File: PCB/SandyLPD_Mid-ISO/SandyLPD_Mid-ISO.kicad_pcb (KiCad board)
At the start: 2 copper layers, 42.5 x 23.2 mm, 30 parts

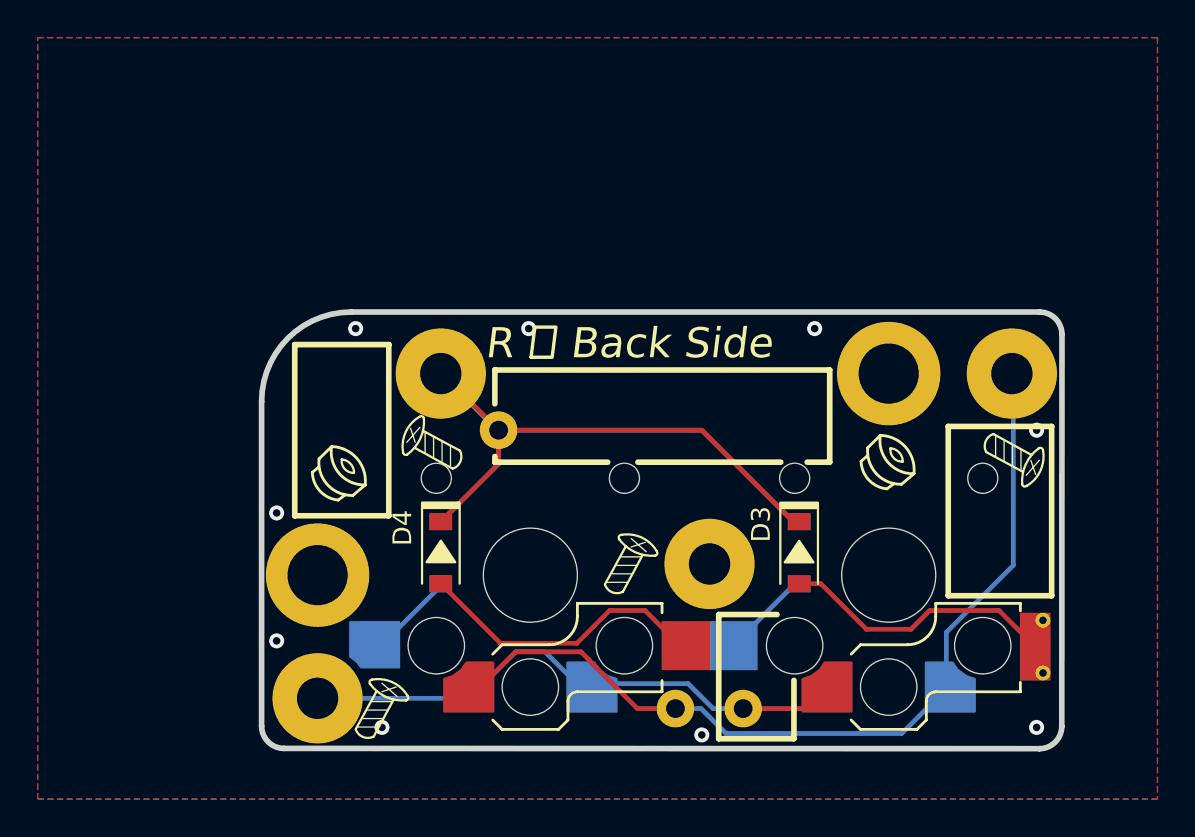
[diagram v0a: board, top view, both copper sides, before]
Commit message: ゴムシート貼り付け指標を調整
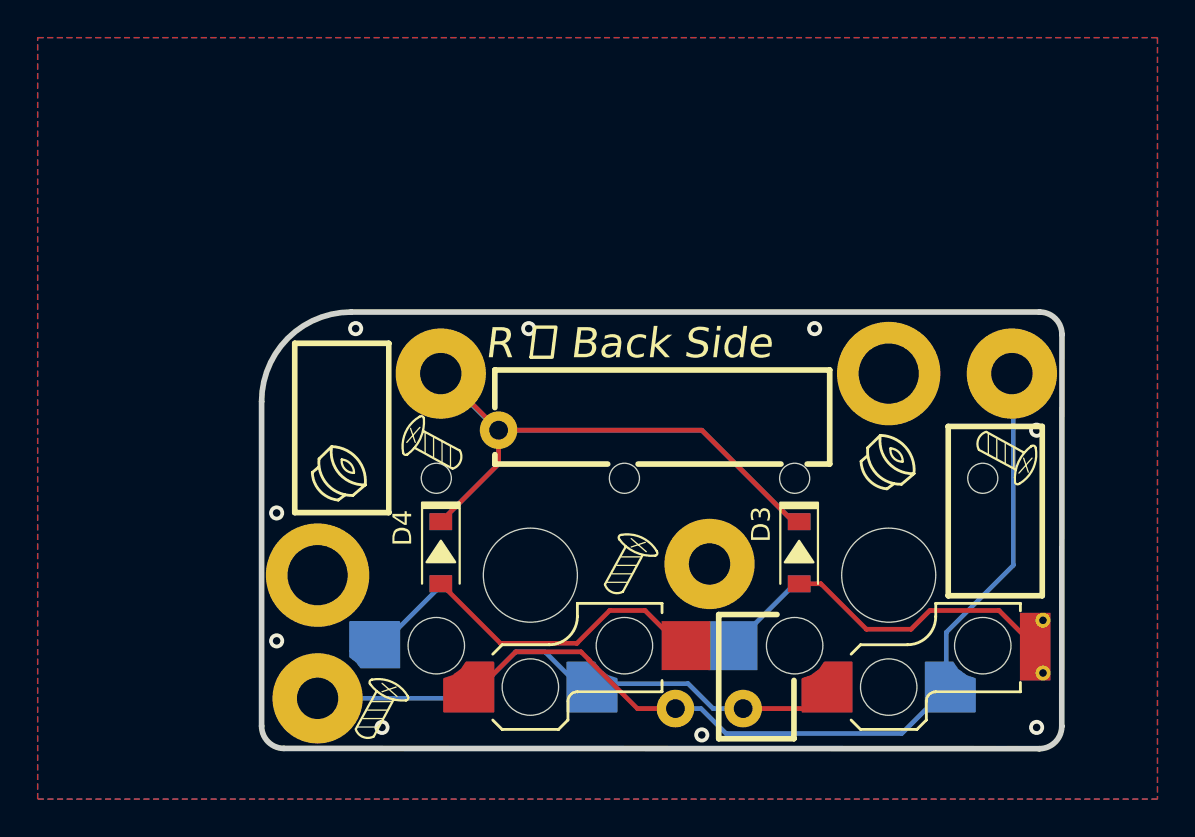
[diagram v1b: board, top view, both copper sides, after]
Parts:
- moved REF** 0.41 mm to (62.9, 43.3)
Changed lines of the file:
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@@
 		(locked yes)
 		(layer "F.Cu")
-		(at 63.241452 43.431721 -90)
+		(at 62.853952 43.312971 -90)
 		(property "Reference" "REF**"
 			(at 0 0.5 90)
@@
 	)
 	(gr_line
-		(start 38.220935 40.51903)
+		(start 38.220935 40.71903)
 		(end 38.220935 38.71903)
 		(stroke
@@
 	)
 	(gr_line
-		(start 38.220935 43.61903)
-		(end 44.220935 43.61903)
+		(start 38.220935 43.71903)
+		(end 44.220935 43.71903)
 		(stroke
 			(width 0.3)
@@
 	)
 	(gr_rect
-		(start 27.583435 37.35028)
-		(end 32.583435 46.45028)
+		(start 27.583435 37.30028)
+		(end 32.583435 46.30028)
 		(stroke
 			(width 0.3)
@@
 	(gr_line
 		(start 65.220935 44.41903)
-		(end 67.820935 44.41903)
+		(end 67.320935 44.41903)
 		(stroke
 			(width 0.3)
@@
 	)
 	(gr_line
-		(start 67.820935 44.41903)
-		(end 67.820935 51.51903)
+		(start 67.320935 44.41903)
+		(end 67.320935 51.40028)
 		(stroke
 			(width 0.3)
@@
 	)
 	(gr_line
-		(start 38.220935 43.31903)
-		(end 38.220935 43.61903)
+		(start 38.220935 43.21903)
+		(end 38.220935 43.71903)
 		(stroke
 			(width 0.3)
@@
 	)
 	(gr_line
-		(start 67.873435 51.36028)
-		(end 67.873435 52.66028)
-		(stroke
-			(width 0.2)
-			(type default)
-		)
-		(layer "B.SilkS")
-	)
-	(gr_line
 		(start 62.320935 53.81903)
 		(end 62.320935 44.41903)
@@
 	)
 	(gr_line
-		(start 45.820935 43.61903)
-		(end 53.420935 43.61903)
+		(start 45.833435 43.71903)
+		(end 53.433435 43.71903)
 		(stroke
 			(width 0.3)
@@
 	)
 	(gr_line
-		(start 54.820935 43.61903)
-		(end 56.020935 43.61903)
+		(start 54.820935 43.71903)
+		(end 56.020935 43.71903)
 		(stroke
 			(width 0.3)
@@
 	)
 	(gr_line
-		(start 67.820935 53.81903)
+		(start 67.333435 53.81903)
 		(end 65.920935 53.81903)
 		(stroke
@@
 	)
 	(gr_line
-		(start 56.020935 43.61903)
+		(start 56.020935 43.71903)
 		(end 56.020935 38.71903)
 		(stroke
@@
 	)
 	(gr_line
-		(start 62.420935 53.81903)
+		(start 62.533435 53.81903)
 		(end 62.320935 53.81903)
 		(stroke
@@
 	)
 	(gr_line
-		(start 67.820935 52.51903)
-		(end 67.820935 53.81903)
+		(start 67.333435 52.65028)
+		(end 67.333435 53.81903)
 		(stroke
 			(width 0.3)
@@
 	)
 	(gr_line
-		(start 38.220935 40.51903)
+		(start 38.220935 40.71903)
 		(end 38.220935 38.71903)
 		(stroke
@@
 	)
 	(gr_line
-		(start 54.820935 43.61903)
-		(end 56.020935 43.61903)
+		(start 54.820935 43.71903)
+		(end 56.020935 43.71903)
 		(stroke
 			(width 0.3)
@@
 	)
 	(gr_line
-		(start 45.820935 43.61903)
-		(end 53.420935 43.61903)
+		(start 45.833435 43.71903)
+		(end 53.433435 43.71903)
 		(stroke
 			(width 0.3)
@@
 	)
 	(gr_line
-		(start 38.220935 43.61903)
-		(end 44.220935 43.61903)
+		(start 38.220935 43.71903)
+		(end 44.220935 43.71903)
 		(stroke
 			(width 0.3)
@@
 	)
 	(gr_rect
-		(start 27.583435 37.36903)
-		(end 32.583435 46.46903)
+		(start 27.583435 37.30028)
+		(end 32.583435 46.30028)
 		(stroke
 			(width 0.3)
@@
 	)
 	(gr_line
-		(start 56.020935 43.61903)
+		(start 56.020935 43.71903)
 		(end 56.020935 38.71903)
 		(stroke
@@
 	)
 	(gr_line
-		(start 38.220935 43.31903)
-		(end 38.220935 43.61903)
+		(start 38.220935 43.21903)
+		(end 38.220935 43.71903)
 		(stroke
 			(width 0.3)
@@
 	(gr_rect
 		(start 62.320935 41.71903)
-		(end 67.820935 50.71903)
+		(end 67.320935 50.71903)
 		(stroke
 			(width 0.3)

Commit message: シルク位置調整 #20
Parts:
- moved REF** 6.38 mm to (63.1, 44.7), turned to 180 degrees
- moved REF** 0.12 mm to (32.6, 54.2)
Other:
- board text added: "L Back"
- board text added: "R Back"
- board text removed: "L 左 Back Side"
- board text removed: "R 右 Back Side"
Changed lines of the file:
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@@
 		(locked yes)
 		(layer "B.Cu")
-		(at 32.633627 54.339547)
+		(at 32.596127 54.220797)
 		(property "Reference" "REF**"
 			(at 0 -0.5 0)
@@
 		(locked yes)
 		(layer "B.Cu")
-		(at 69.000419 42.331722 -90)
+		(at 63.070744 44.679764 180)
 		(property "Reference" "REF**"
-			(at 0 -0.5 90)
+			(at 0 -0.5 360)
 			(layer "Cmts.User")
 			(effects
@@
 		)
 		(property "Value" "ICON_Screw_Medium"
-			(at 0 0.5 90)
+			(at 0 0.5 360)
 			(layer "B.Fab")
 			(effects
@@
 		)
 		(property "Footprint" "locallib:ICON_Screw_Medium"
-			(at 0 0 90)
+			(at 0 0 360)
 			(layer "B.Fab")
 			(hide yes)
@@
 		)
 		(property "Datasheet" ""
-			(at 0 0 90)
+			(at 0 0 360)
 			(layer "B.Fab")
 			(hide yes)
@@
 		)
 		(property "Description" ""
-			(at 0 0 90)
+			(at 0 0 360)
 			(layer "B.Fab")
 			(hide yes)
@@
 		)
 		(attr through_hole board_only)
+		(fp_line
+			(start 0.889799 3.224953)
+			(end 0.089799 3.924953)
+			(stroke
+				(width 0.06)
+				(type solid)
+			)
+			(layer "B.SilkS")
+		)
+		(fp_line
+			(start 0.7 3.05)
+			(end -0.35 1.1)
+			(stroke
+				(width 0.12)
+				(type solid)
+			)
+			(layer "B.SilkS")
+		)
+		(fp_line
+			(start 0.6 2.95)
+			(end -0.45 2.95)
+			(stroke
+				(width 0.06)
+				(type solid)
+			)
+			(layer "B.SilkS")
+		)
+		(fp_line
+			(start 0.375 2.5)
+			(end -0.675 2.5)
+			(stroke
+				(width 0.06)
+				(type solid)
+			)
+			(layer "B.SilkS")
+		)
+		(fp_line
+			(start 0.125 2.05)
+			(end -0.925 2.05)
+			(stroke
+				(width 0.06)
+				(type solid)
+			)
+			(layer "B.SilkS")
+		)
 		(fp_line
 			(start 0.089799 3.474953)
@@
 		)
 		(fp_line
-			(start 0.889799 3.224953)
-			(end 0.089799 3.924953)
-			(stroke
-				(width 0.06)
-				(type solid)
-			)
-			(layer "B.SilkS")
-		)
-		(fp_line
-			(start 0.7 3.05)
-			(end -0.35 1.1)
-			(stroke
-				(width 0.12)
-				(type solid)
-			)
-			(layer "B.SilkS")
-		)
-		(fp_line
-			(start 0.6 2.95)
-			(end -0.45 2.95)
-			(stroke
-				(width 0.06)
-				(type solid)
-			)
-			(layer "B.SilkS")
-		)
-		(fp_line
-			(start 0.375 2.5)
-			(end -0.675 2.5)
-			(stroke
-				(width 0.06)
-				(type solid)
-			)
-			(layer "B.SilkS")
-		)
-		(fp_line
-			(start 0.125 2.05)
-			(end -0.925 2.05)
-			(stroke
-				(width 0.06)
-				(type solid)
-			)
-			(layer "B.SilkS")
-		)
-		(fp_line
 			(start -0.125 1.6)
 			(end -1.175 1.6)
@@
 				(width 0.12)
 				(type solid)
+			)
+			(layer "B.SilkS")
+		)
+		(fp_arc
+			(start 1.451182 3.252804)
+			(mid 0.638942 3.98345)
+			(end -0.445 4.119999)
+			(stroke
+				(width 0.12)
+				(type solid)
+			)
+			(layer "B.SilkS")
+		)
+		(fp_arc
+			(start 1.365506 3.013511)
+			(mid 1.47525 3.107646)
+			(end 1.447466 3.249538)
+			(stroke
+				(width 0.12)
+				(type default)
 			)
 			(layer "B.SilkS")
@@
 				(width 0.12)
 				(type solid)
-			)
-			(layer "B.SilkS")
-		)
-		(fp_arc
-			(start 1.451182 3.252804)
-			(mid 0.638942 3.98345)
-			(end -0.445 4.119999)
-			(stroke
-				(width 0.12)
-				(type solid)
-			)
-			(layer "B.SilkS")
-		)
-		(fp_arc
-			(start 1.365506 3.013511)
-			(mid 1.47525 3.107646)
-			(end 1.447466 3.249538)
-			(stroke
-				(width 0.12)
-				(type default)
 			)
 			(layer "B.SilkS")
@@
 		(layer "F.SilkS")
 	)
-	(gr_text "L 左 Back Side"
-		(at 56.383435 37.30028 0)
+	(gr_text "L Back"
+		(at 54.395955 41.290906 0)
 		(layer "B.SilkS" knockout)
 		(effects
@@
 		)
 	)
-	(gr_text "#SandyLP_Duo\nDN0010"
-		(at 54.991268 41.290906 0)
+	(gr_text "#SandyLP_Duo DN0010"
+		(at 55.783435 37.70028 0)
 		(layer "B.SilkS")
 		(effects
@@
 		)
 	)
-	(gr_text "R 右 Back Side"
-		(at 37.683435 37.30028 0)
+	(gr_text "R Back"
+		(at 46.061573 41.290906 0)
 		(layer "F.SilkS" knockout)
 		(effects

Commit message: ネジ等の3Dモデル追加
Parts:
- H1, H2, H3, H4: footprint locallib:MountingHole_2.2-4.8mm_M2_Pad_minimal_for_Through-hole_tap -> locallib:MountingHole_2.2-4.8mm_M2_Pad_minimal_for_Through-hole_tap_L3mm; moved to F.Cu
- H5, H6: footprint locallib:MountingHole_M2_Through-hole_tap_THC-0.8-x-2 -> locallib:MountingHole_M2_Through-hole_tap_THC-0.8-1.0-2
- turned H1 to 180 degrees
- turned H2 to 0 degrees
- turned H3 to 180 degrees
- turned H4 to 0 degrees
